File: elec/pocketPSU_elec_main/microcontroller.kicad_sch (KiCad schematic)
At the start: 0 parts

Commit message: add esp32 micro
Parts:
- added C10, C9: 10uF, symbol Device:C_Small
- added C11, C12, C13: 100nF, symbol Device:C_Small
- added R11: 10K, symbol Device:R_Small
- added SW6: TS-1187A-B-A-B, footprints:SW-SMD_4P-L5.1-W5.1-P3.70-LS6.5-TL-2, symbol footprints:TS-1187A-B-A-B
- added U2: ESP32-S3-WROOM-1(N16R2), footprints:WIRELM-SMD_ESP32-S3-WROOM-1, symbol footprints:ESP32-S3-WROOM-1(N16R2)
- added U3: AMS1117-3.3, footprints:SOT-223-3_L6.5-W3.4-P2.30-LS7.0-BR, symbol footprints:AMS1117-3.3
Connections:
- new net: R11.2, SW6.2 (B), SW6.4 (D), U2.3 (EN)
- new net +3.3V: C10.1, C11.1, C12.1, C9.1, R11.1, U2.2 (3V3), U3.2 (VOUT), U3.4 (VOUT)
- new net BT_1: U2.4 (IO4)
- new net BT_2: U2.5 (IO5)
- new net BT_3: U2.6 (IO6)
- new net BT_4: U2.7 (IO7)
- new net ENCODER_A: U2.39 (IO1)
- new net ENCODER_B: U2.38 (IO2)
- new net ENCODER_BT: U2.15 (IO3)
- new net GND: C10.2, C11.2, C12.2, C13.2, C9.2, SW6.1 (A), SW6.3 (C), U2.1 (GND), U2.40 (GND), U2.41 (GND), U3.1 (GND)
- new net SCREEN_BACKLIGHT_EN: U2.8 (IO15)
- new net SPI_CS: U2.18 (IO10)
- new net SPI_MISO: U2.21 (IO13)
- new net SPI_MOSI: U2.19 (IO11)
- new net SPI_SCK: U2.20 (IO12)
- new net USB_DM: U2.13 (IO19)
- new net USB_DP: U2.14 (IO20)
- new net VBUS: C13.1, U3.3 (VIN)
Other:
- title: (none) -> Microcontroller

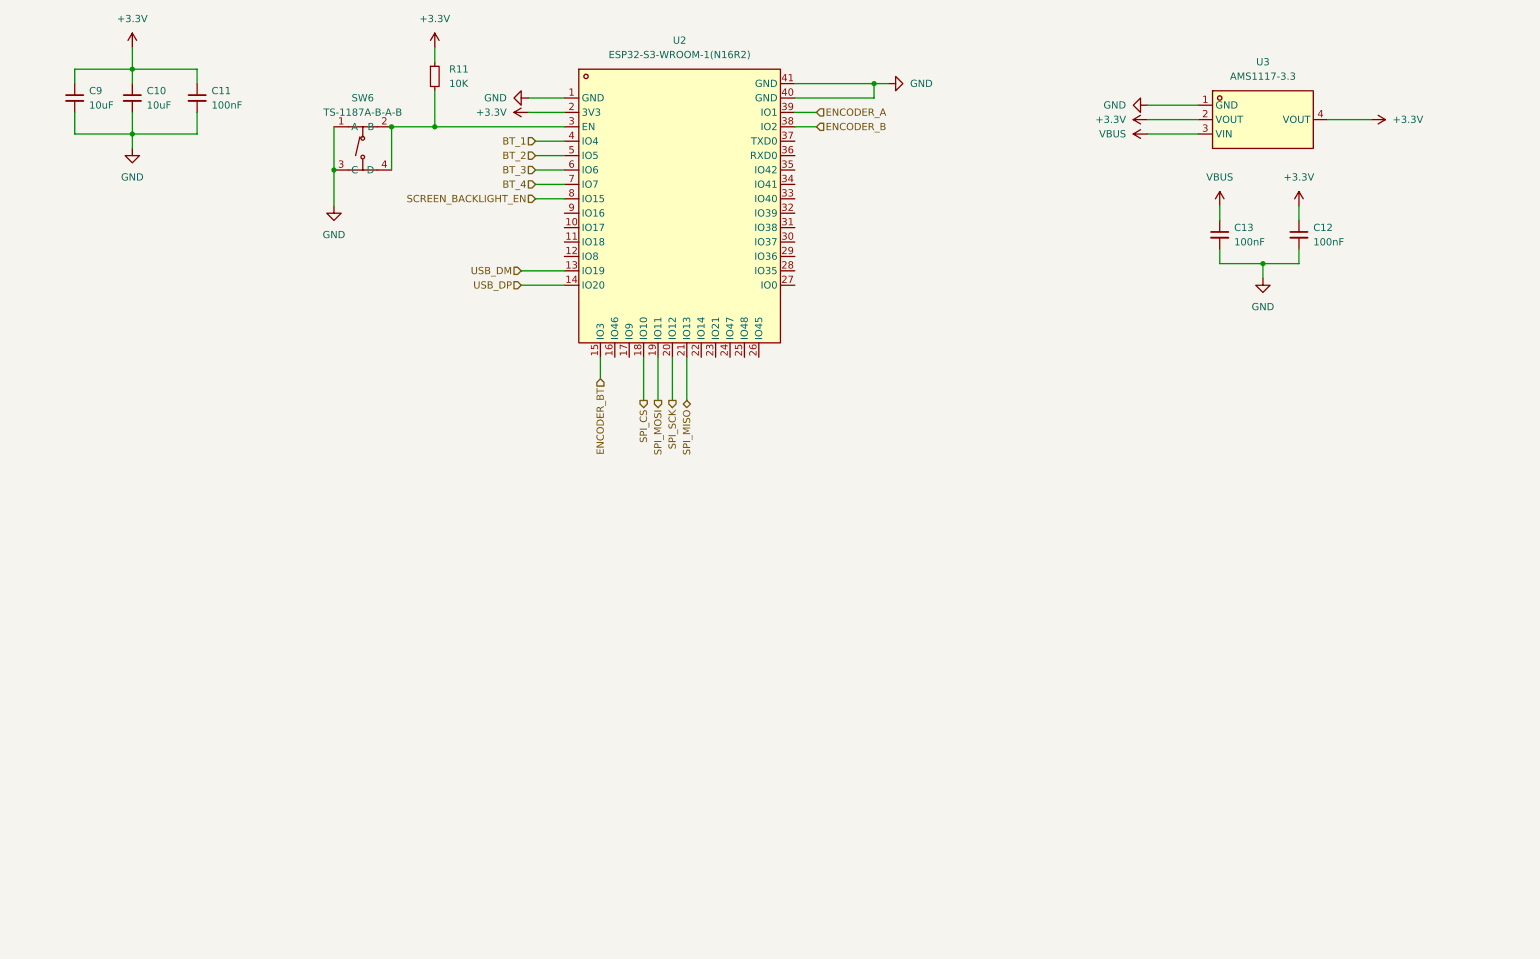
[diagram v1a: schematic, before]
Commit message: Add footprints, change TFT hookup
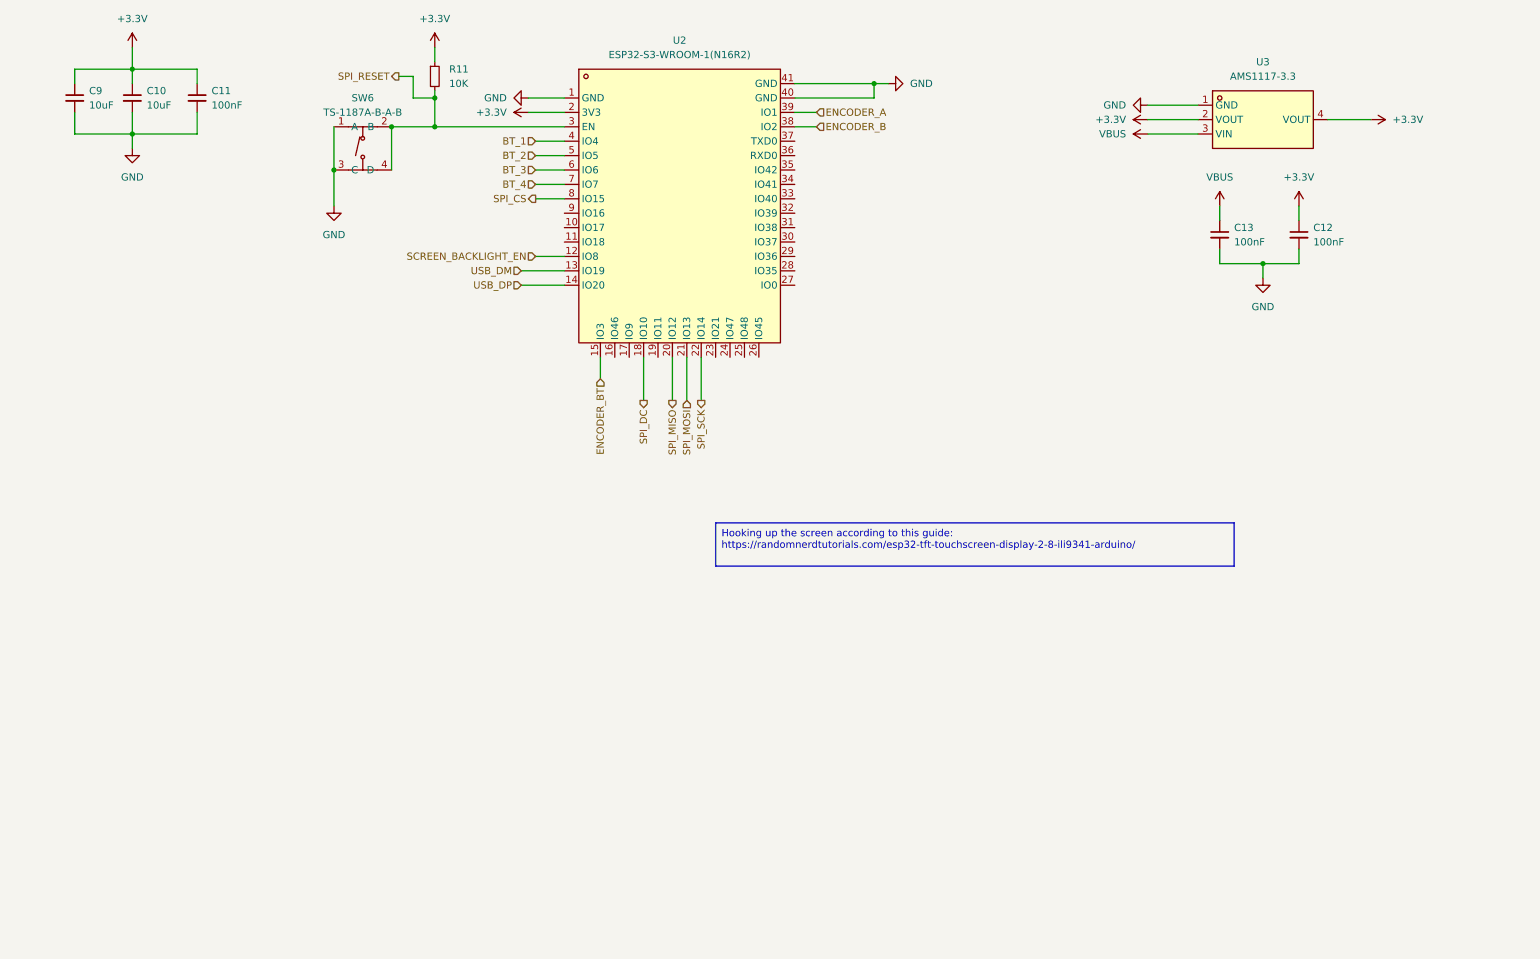
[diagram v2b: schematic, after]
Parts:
- C10, C11, C9: footprint (none) -> Capacitor_SMD:C_0805_2012Metric
- C12, C13: footprint (none) -> Capacitor_SMD:C_0805_2012Metric; LCSC Part (none) -> C49678
- R11: footprint (none) -> Resistor_SMD:R_0402_1005Metric
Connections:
- net SCREEN_BACKLIGHT_EN: now also U2.12 (IO8); no longer U2.8 (IO15)
- net SPI_CS: now also U2.8 (IO15); no longer U2.18 (IO10)
- net SPI_MISO: now also U2.20 (IO12); no longer U2.21 (IO13)
- net SPI_MOSI: now also U2.21 (IO13); no longer U2.19 (IO11)
- net SPI_SCK: now also U2.22 (IO14); no longer U2.20 (IO12)
- net SPI_RESET: now reaches R11.2, SW6.2 (B), SW6.4 (D), U2.3 (EN)
- new net SPI_DC: U2.18 (IO10)

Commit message: add usb coms chip
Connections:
- net USB_SDA: now reaches U2.28 (IO35)
- net USB_SCL: now reaches U2.29 (IO36)
- net USB_INT_N: now reaches U2.30 (IO37)
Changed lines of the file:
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@@
+	(wire
+		(pts
+			(xy 157.48 63.5) (xy 161.29 63.5)
+		)
+		(stroke
+			(width 0)
+			(type default)
+		)
+	)
 	(wire
 		(pts
@@
 	(wire
 		(pts
+			(xy 157.48 68.58) (xy 161.29 68.58)
+		)
+		(stroke
+			(width 0)
+			(type default)
+		)
+	)
+	(wire
+		(pts
 			(xy 40.64 29.21) (xy 40.64 33.02)
 		)
@@
 		(pts
 			(xy 240.03 67.31) (xy 240.03 69.85)
+		)
+		(stroke
+			(width 0)
+			(type default)
+		)
+	)
+	(wire
+		(pts
+			(xy 157.48 66.04) (xy 161.29 66.04)
 		)
 		(stroke
@@
 		)
 	)
+	(hierarchical_label "USB_SDA"
+		(shape bidirectional)
+		(at 161.29 68.58 0)
+		(fields_autoplaced yes)
+		(effects
+			(font
+				(size 1.27 1.27)
+			)
+			(justify left)
+		)
+	)
+	(hierarchical_label "USB_INT_N"
+		(shape bidirectional)
+		(at 161.29 63.5 0)
+		(fields_autoplaced yes)
+		(effects
+			(font
+				(size 1.27 1.27)
+			)
+			(justify left)
+		)
+	)
 	(hierarchical_label "SPI_DC"
 		(shape output)
@@
 		)
 	)
+	(hierarchical_label "USB_SCL"
+		(shape output)
+		(at 161.29 66.04 0)
+		(fields_autoplaced yes)
+		(effects
+			(font
+				(size 1.27 1.27)
+			)
+			(justify left)
+		)
+	)

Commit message: fix caps values, rework layout
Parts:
- added LED2: KT-0603R, footprints:LED0603-RD, symbol footprints:KT-0603R
- added R15, R16: 100R, Resistor_SMD:R_0402_1005Metric, symbol Device:R_Small
- added U5: F.0603.00026/P2-0603B1TS2-06T-001, footprints:LED0603-RD, symbol footprints:F.0603.00026_P2-0603B1TS2-06T-001
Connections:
- net +3.3V: now also U5.2 (A)
- net GND: now also R15.2, R16.2
- net BLINKY_LED: now reaches U2.17 (IO9)
- net BLINKY_LED: now also LED2.2 (A)
- new net: R15.1, U5.1 (K)
- new net: LED2.1 (K), R16.1
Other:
- moved on the sheet: C12, C13

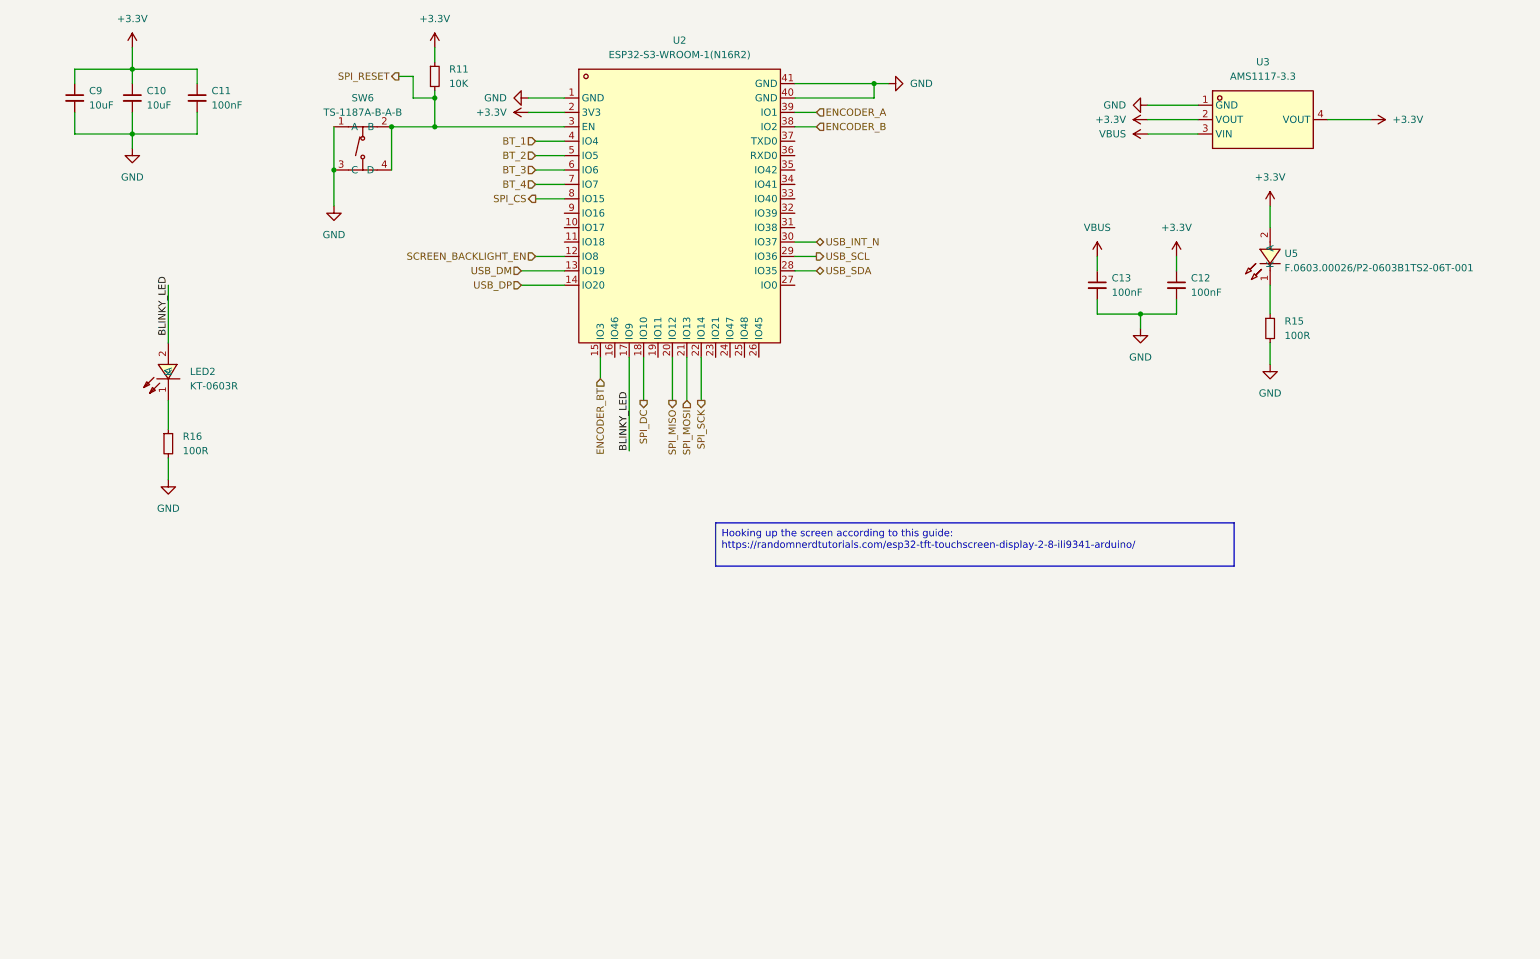
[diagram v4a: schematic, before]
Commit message: add boot switch and test points
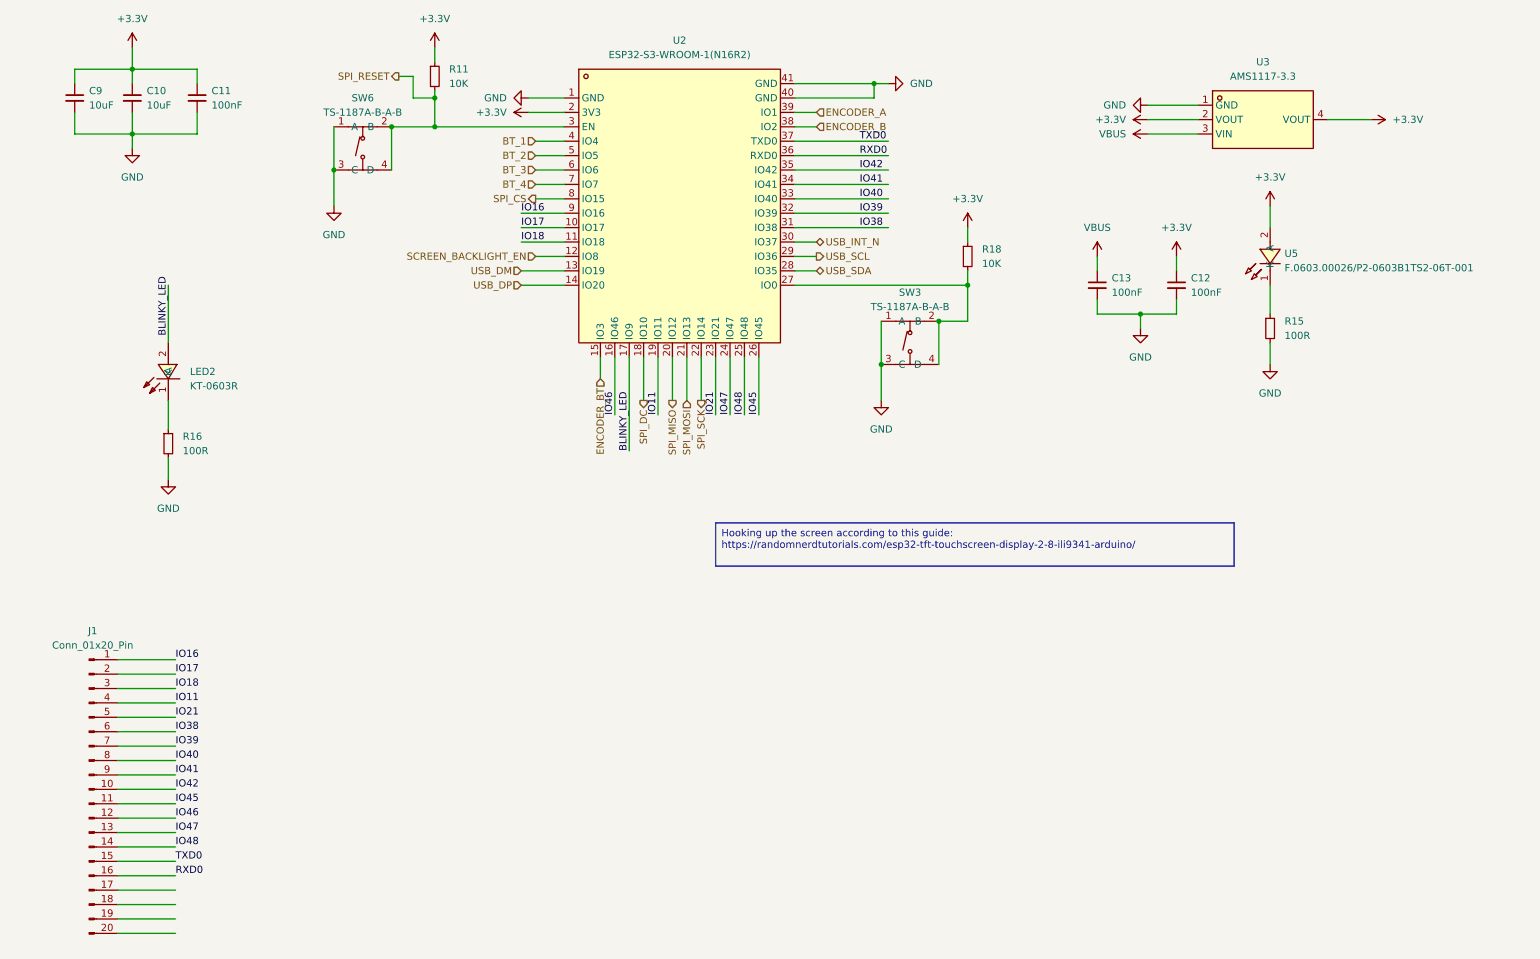
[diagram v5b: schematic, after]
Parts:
- added J1: Conn_01x20_Pin, Connector_PinHeader_1.27mm:PinHeader_1x20_P1.27mm_Vertical, symbol Connector:Conn_01x20_Pin
- added R18: 10K, Resistor_SMD:R_0402_1005Metric, symbol Device:R_Small
- added SW3: TS-1187A-B-A-B, footprints:SW-SMD_4P-L5.1-W5.1-P3.70-LS6.5-TL-2, symbol footprints:TS-1187A-B-A-B
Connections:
- net +3.3V: now also R18.1
- net GND: now also SW3.1 (A), SW3.3 (C)
- net IO17: now reaches U2.10 (IO17)
- net IO17: now also J1.2 (Pin_2)
- net IO18: now reaches U2.11 (IO18)
- net IO18: now also J1.3 (Pin_3)
- net IO46: now reaches U2.16 (IO46)
- net IO46: now also J1.12 (Pin_12)
- net IO11: now reaches U2.19 (IO11)
- net IO11: now also J1.4 (Pin_4)
- net IO21: now reaches U2.23 (IO21)
- net IO21: now also J1.5 (Pin_5)
- net IO47: now reaches U2.24 (IO47)
- net IO47: now also J1.13 (Pin_13)
- net IO48: now reaches U2.25 (IO48)
- net IO48: now also J1.14 (Pin_14)
- net IO45: now reaches U2.26 (IO45)
- net IO45: now also J1.11 (Pin_11)
- net at U2.27 (IO0): now also R18.2, SW3.2 (B), SW3.4 (D)
- net IO38: now reaches U2.31 (IO38)
- net IO38: now also J1.6 (Pin_6)
- net IO39: now reaches U2.32 (IO39)
- net IO39: now also J1.7 (Pin_7)
- net IO40: now reaches U2.33 (IO40)
- net IO40: now also J1.8 (Pin_8)
- net IO41: now reaches U2.34 (IO41)
- net IO41: now also J1.9 (Pin_9)
- net IO42: now reaches U2.35 (IO42)
- net IO42: now also J1.10 (Pin_10)
- net RXD0: now reaches U2.36 (RXD0)
- net RXD0: now also J1.16 (Pin_16)
- net TXD0: now reaches U2.37 (TXD0)
- net TXD0: now also J1.15 (Pin_15)
- net IO16: now reaches U2.9 (IO16)
- net IO16: now also J1.1 (Pin_1)
